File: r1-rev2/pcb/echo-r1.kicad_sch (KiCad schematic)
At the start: 96 parts, among them J2 TYPE-C-31-M-12, J3 TF-115, J6 Conn_01x05, J7 ILI9342C, J8 Conn_01x04, Q4 AO3401A, Q5 AO3401A, SW1 A, SW10 SELECT, SW11 VOL+, SW12 VOL-, SW13 POWER, SW14 HOLD, SW2 B, SW3 X, SW4 Y, SW5 DPAD↑, SW6 DPAD↓, SW7 DPAD←, SW8 DPAD→, SW9 START, U10 TPAZ1143-04F, U11 TPAZ1143-04F, U12 TPAZ1143-04F, U14 USBLC6-2SC6, U7 STM32H7R3Z8Jx, U8 W958D8NBYA5I, U9 TPAZ1143-04F, Y1 SC-32S32.768kHz20PPM12.5pF, Y2 XTM32024000JT00351001

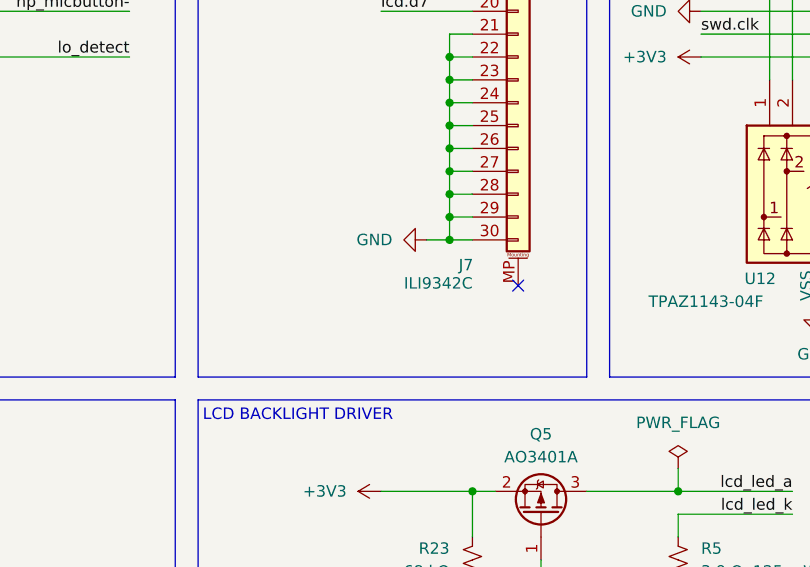
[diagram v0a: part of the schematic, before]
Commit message: R1-Rev2: add LCD ribbon connector
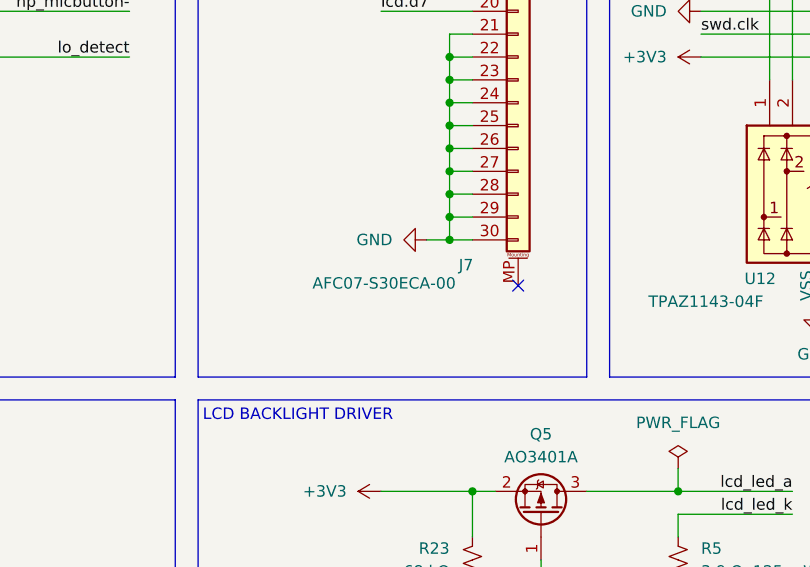
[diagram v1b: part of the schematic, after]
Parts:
- J7: value ILI9342C -> AFC07-S30ECA-00; footprint (none) -> echoplayer:Conn_Jushuo_AFC07-S30ECA-00_RTL

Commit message: R1-Rev2: updates to PCB layout, add HyperRAM routing
- Reannotate schematic and assign footprints for passives
- First try at HyperRAM routing
- Fixed incorrect W958D8NBYA5I pinout
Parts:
- C1: renamed from C9; value 5 pF/NP0 -> 10 pF
- C2: renamed from C11; value 5 pF/NP0 -> 10 pF
- C28: renamed from C26; footprint Capacitor_SMD:C_0805_2012Metric -> Capacitor_SMD:C_0402_1005Metric
- C3: renamed from C10; value 4 pF/NP0 -> 10 pF
- C39: renamed from C77; footprint Capacitor_SMD:C_0402_1005Metric -> Capacitor_SMD:C_0805_2012Metric
- C4: renamed from C12; value 4 pF/NP0 -> 10 pF
- C40: renamed from C76; footprint Capacitor_SMD:C_0402_1005Metric -> Capacitor_SMD:C_0805_2012Metric
- C41: renamed from C70; footprint Capacitor_SMD:C_0402_1005Metric -> Capacitor_SMD:C_0805_2012Metric
- C42: renamed from C60; footprint Capacitor_SMD:C_0402_1005Metric -> Capacitor_SMD:C_0805_2012Metric
- C47: renamed from C79; footprint Capacitor_SMD:C_0402_1005Metric -> Capacitor_SMD:C_0805_2012Metric
- C48: renamed from C71; footprint Capacitor_SMD:C_0402_1005Metric -> Capacitor_SMD:C_0805_2012Metric
- C55: renamed from C13; footprint Capacitor_SMD:C_0603_1608Metric -> Capacitor_SMD:C_0805_2012Metric
- NT4: renamed from NT3; footprint (none) -> echoplayer:NetTie_0.15mm_SMD
- NT5: renamed from NT4; footprint (none) -> echoplayer:NetTie_0.15mm_SMD
- R1: renamed from R5; footprint Resistor_SMD:R_0402_1005Metric -> Resistor_SMD:R_0805_2012Metric
- R10: footprint Resistor_SMD:R_0603_1608Metric -> Resistor_SMD:R_0402_1005Metric
- R2: renamed from R12; footprint Resistor_SMD:R_0603_1608Metric -> Resistor_SMD:R_0402_1005Metric
- R7: renamed from R13; footprint Resistor_SMD:R_0603_1608Metric -> Resistor_SMD:R_0402_1005Metric
- renumbered C74 to C10, C61 to C11, C63 to C12, C68 to C13, C32 to C14, C56 to C15, C57 to C16, C33 to C17, C58 to C18, C65 to C19, C59 to C20, C66 to C21, C73 to C22, C78 to C23, C75 to C29, C62 to C30, C64 to C31, C69 to C32, C67 to C33, C42 to C5, C83 to C6, C82 to C7, C81 to C8, C80 to C9, J2 to J1, J3 to J2, J7 to J6, J8 to J7, J6 to J8, L3 to L1, NT5 to NT1, NT7 to NT2, NT6 to NT3, Q5 to Q1, Q4 to Q2, R25 to R14, R2 to R15, R22 to R16, R23 to R17, R3 to R18, R15 to R5, R14 to R6, R26 to R8, R27 to R9, U7 to U1, U14 to U10, U9 to U11, U10 to U12, U11 to U13, U12 to U14, U8 to U2
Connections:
- net xspi.ck-: now also U2.B1 (CK#); no longer U2.A2 (CK#)

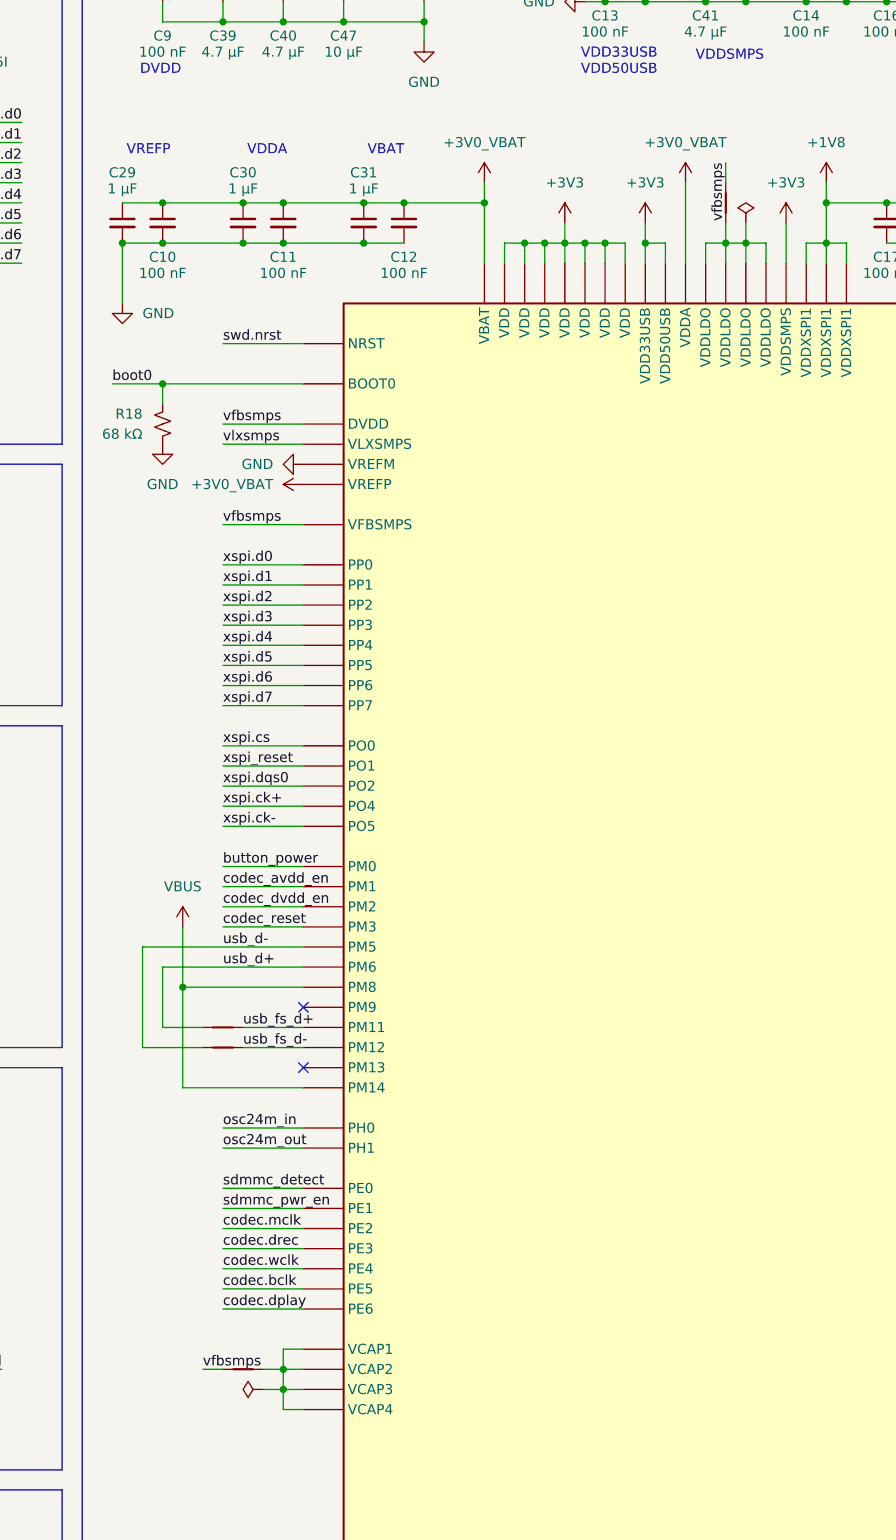
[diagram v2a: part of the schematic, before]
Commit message: R1-Rev2: update USB D+/D- net ties to avoid USBHS stubs
The USB data lines have to be routed to both HS and FS PHYs
since only the FS PHY supports DFU mode. To minimize stub
length in HS operation, the data lines from the connector
should route through the FS pins first and terminate at the
HS pins.
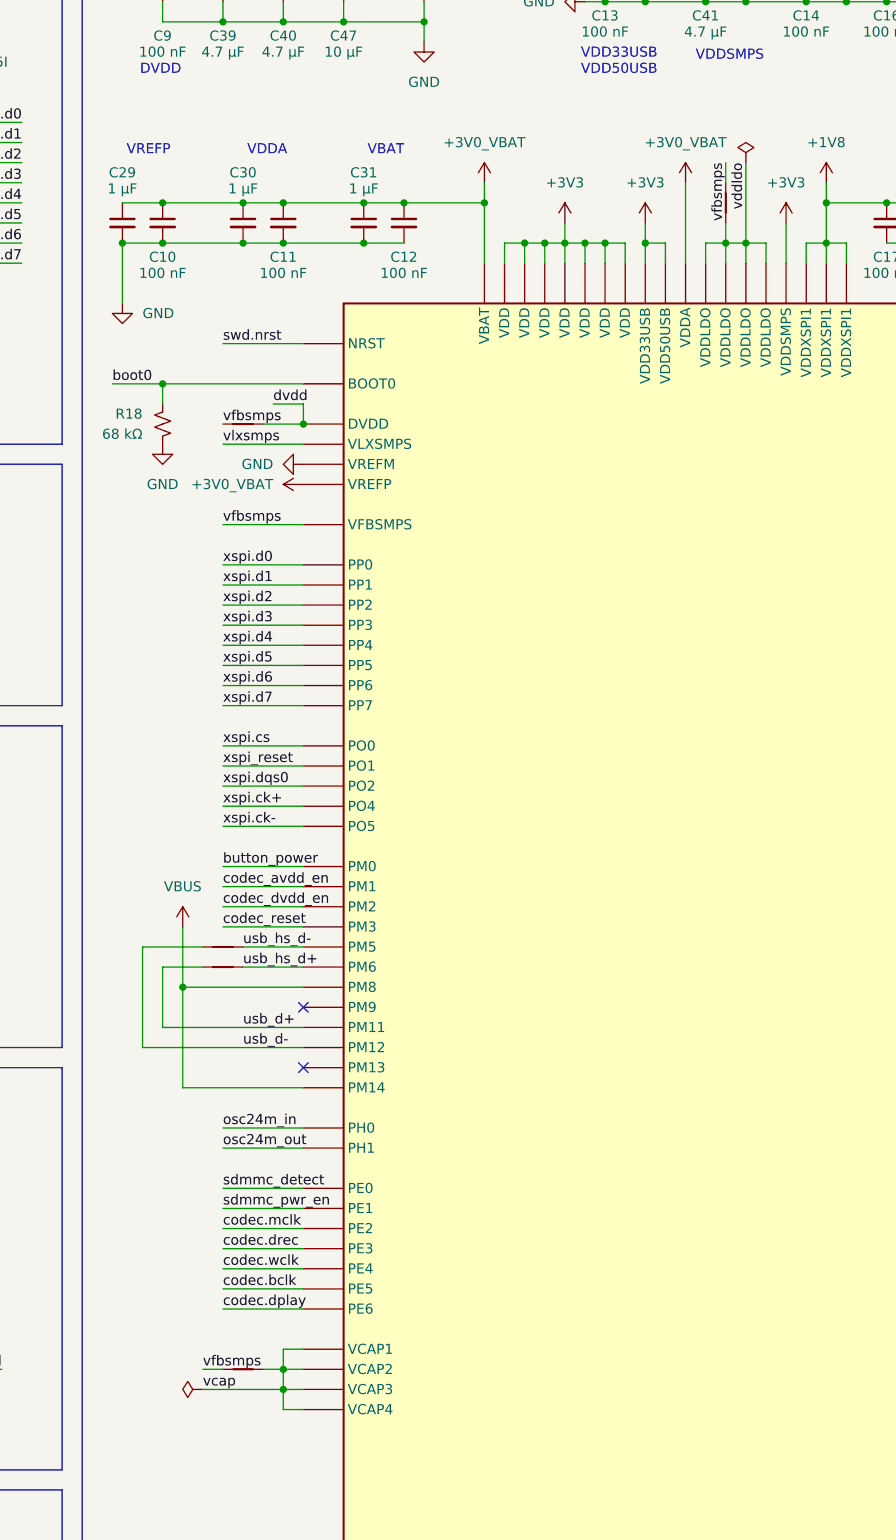
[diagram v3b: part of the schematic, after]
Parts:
- removed NT2, NT3: NetTie_2, echoplayer:NetTie_0.15mm_SMD, symbol Device:NetTie_2
- added NT10: NetTie_2, echoplayer:NetTie_0.15mm_SMD, symbol Device:NetTie_2
- added NT8, NT9: NetTie_2, echoplayer:NetTie_0.10mm_SMD, symbol Device:NetTie_2
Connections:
- net usb_fs_d+ is gone; now on net usb_d+: U1.A7 (PM11)
- net usb_fs_d- is gone; now on net usb_d-: U1.B7 (PM12)
- net usb_d+: now also NT9.1; no longer U1.A9 (PM6)
- net usb_d-: now also NT8.1; no longer U1.B9 (PM5)
- net vfbsmps: now also NT10.1; no longer U1.C8 (DVDD)
- net vddldo: now reaches NT5.2, U1.F6 (VDDLDO), U1.F7 (VDDLDO), U1.G6 (VDDLDO), U1.G7 (VDDLDO)
- net vcap: now reaches NT4.2, U1.E5 (VCAP4), U1.F8 (VCAP3), U1.H6 (VCAP1), U1.H8 (VCAP2)
- new net dvdd: NT10.2, U1.C8 (DVDD)
- new net usb_hs_d+: NT9.2, U1.A9 (PM6)
- new net usb_hs_d-: NT8.2, U1.B9 (PM5)

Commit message: R1-Rev2: add inductor footprint and group components
Also use the same 2.2uH inductor for the buck converters,
to minimize unique component count.
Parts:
- L1: footprint (none) -> Inductor_SMD:L_Changjiang_FNR3015S

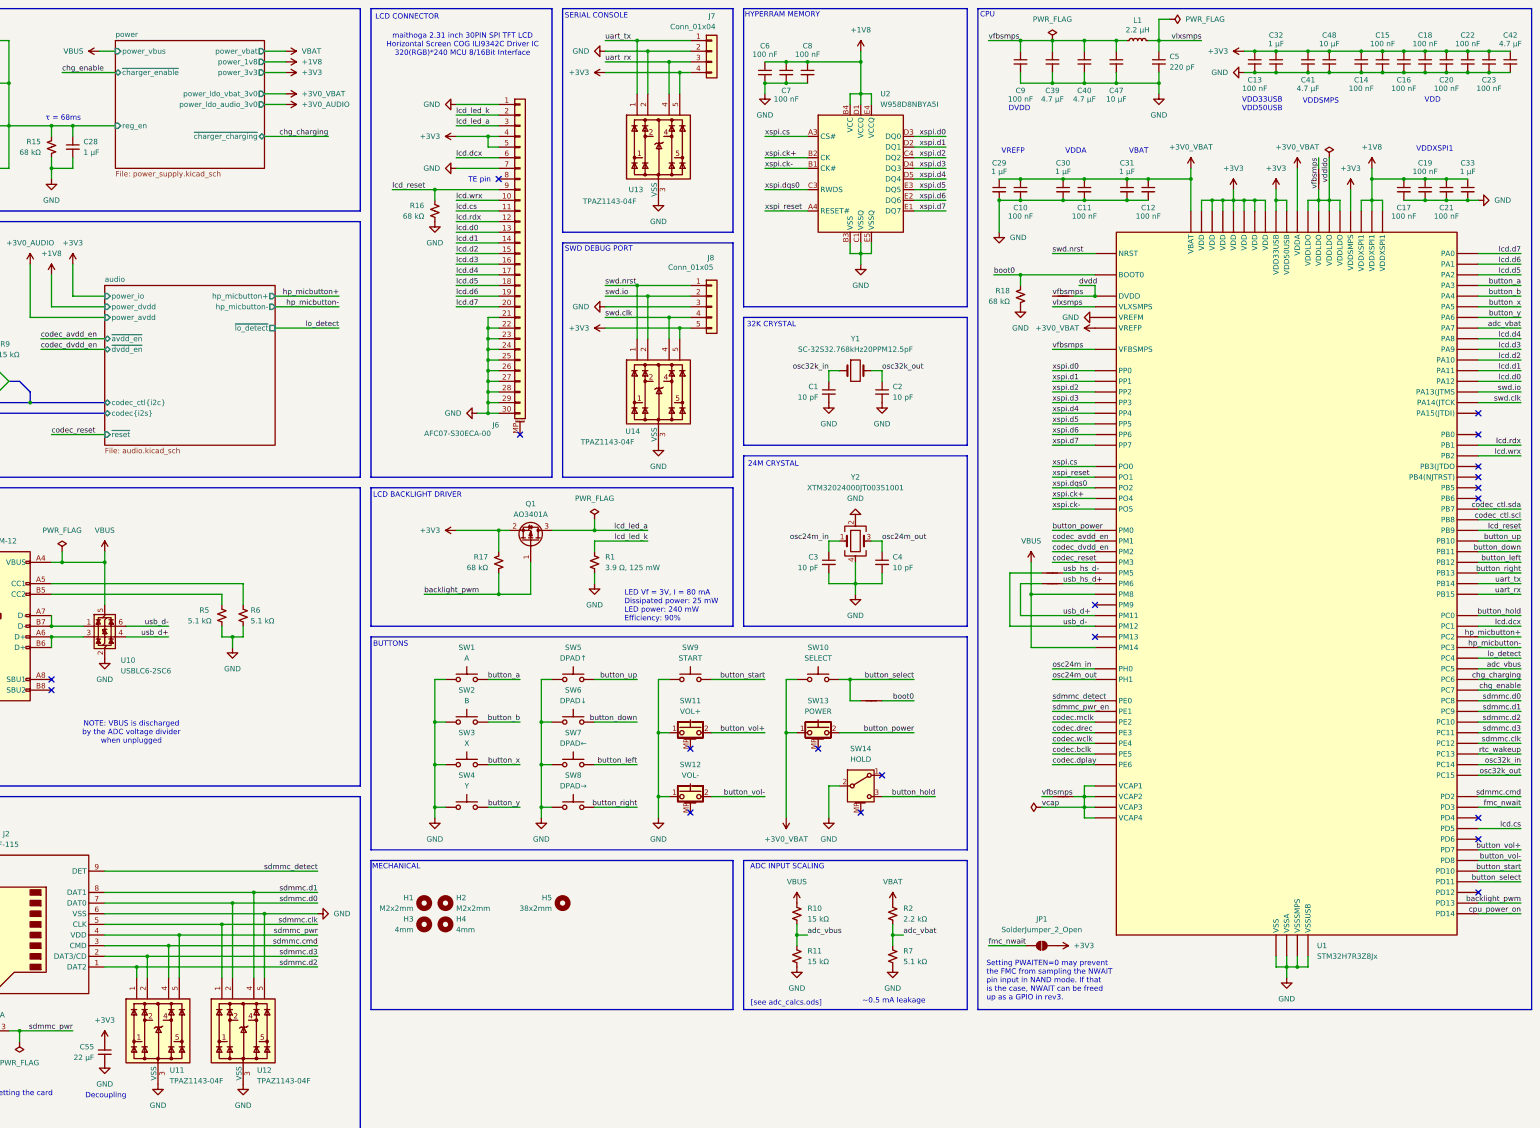
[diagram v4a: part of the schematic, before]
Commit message: R1-Rev2: improve reset circuit, add XSPI CS pullup
Connect NRST to xspi_reset and the regulator power-good signals.
This should ensure that the STM32 and RAM will stay in reset
until both power rails have started up. It shouldn't be necessary
to control xspi_reset with a GPIO, but for now leave it connected
just in case.

The XSPI CS pin also requires an external pullup to guarantee it
will be pulled high during power-on, which is required to ensure
the RAM resets properly.
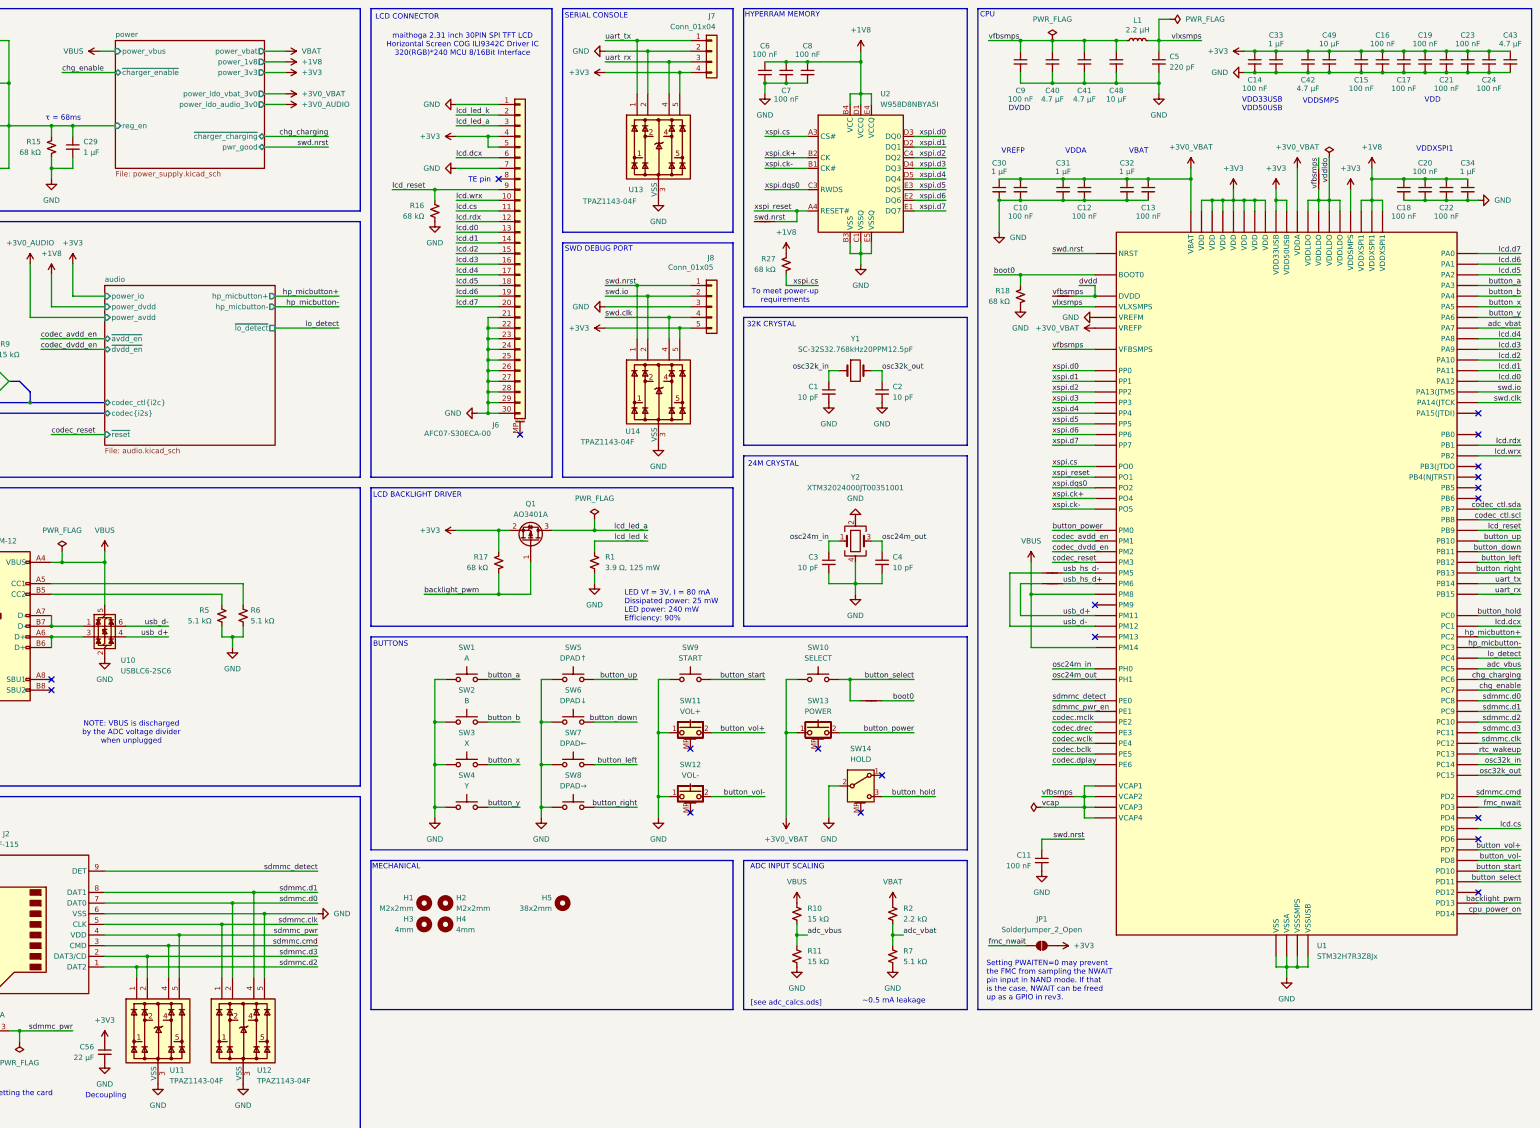
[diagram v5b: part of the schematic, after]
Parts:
- added C11: 100 nF, Capacitor_SMD:C_0402_1005Metric, symbol Device:C_Small
- added NT11: NetTie_2, echoplayer:NetTie_0.15mm_SMD, symbol Device:NetTie_2
- added R27: 68 kΩ, Resistor_SMD:R_0402_1005Metric, symbol Device:R_Small_US
- renumbered C11 to C12, C12 to C13, C13 to C14, C14 to C15, C15 to C16, C16 to C17, C17 to C18, C18 to C19, C19 to C20, C20 to C21, C21 to C22, C22 to C23, C23 to C24, C28 to C29, C29 to C30, C30 to C31, C31 to C32, C32 to C33, C33 to C34, C39 to C40, C40 to C41, C41 to C42, C42 to C43, C47 to C48, C48 to C49, C55 to C56
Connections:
- net +1V8: now also R27.1
- net GND: now also C11.2
- net swd.nrst: now also C11.1, NT11.1
- net xspi.cs: now also R27.2
- net xspi_reset: now also NT11.2
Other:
- sheet power ports: added pwr_good; removed none
- note added: "To meet power-up requirements"
